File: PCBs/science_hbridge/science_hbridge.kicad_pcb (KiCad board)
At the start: 2 copper layers, 50.6 x 45 mm, 32 parts, among them J1 Conn_02x07_Odd_Even, J2 Conn_02x08_Odd_Even, J3 Conn_02x08_Odd_Even, J4 Conn_01x02_Pin, J5 Conn_01x02_Pin, J6 Conn_01x02_Pin, J7 Conn_01x04_Pin, U1 L298N, U2 MAX485E, U3 NCP718xSN500

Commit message: fixed errors, need to add quadrature
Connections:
- C1 pad 1: +5V -> +24V
- C2 pad 1: +5V -> +24V
- C6 pad 1: +24V -> +5V
- D5 pad 1: +5V -> +24V
- D6 pad 1: +5V -> +24V
- D7 pad 1: +5V -> +24V
- D8 pad 1: +5V -> +24V
- U1 pad 4: +5V -> +24V
- U1 pad 9: +24V -> +5V
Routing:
- net +5V: track 132.1 -> 128.7 mm
- net +24V: track 41.1 -> 41.8 mm
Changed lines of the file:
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@@
 			(layers "F.Cu" "F.Mask" "F.Paste")
 			(roundrect_rratio 0.25)
-			(net 47 "+5V")
+			(net 48 "+24V")
 			(pinfunction "K")
 			(pintype "passive")
@@
 			(layers "*.Cu" "*.Mask")
 			(remove_unused_layers no)
-			(net 47 "+5V")
+			(net 48 "+24V")
 			(pintype "passive")
 		)
@@
 			(layers "*.Cu" "*.Mask")
 			(remove_unused_layers no)
-			(net 47 "+5V")
+			(net 48 "+24V")
 			(pinfunction "Vs")
 			(pintype "power_in")
@@
 			(layers "*.Cu" "*.Mask")
 			(remove_unused_layers no)
-			(net 48 "+24V")
+			(net 47 "+5V")
 			(pinfunction "Vss")
 			(pintype "power_in")
@@
 			(layers "F.Cu" "F.Mask" "F.Paste")
 			(roundrect_rratio 0.25)
-			(net 47 "+5V")
+			(net 48 "+24V")
 			(pinfunction "K")
 			(pintype "passive")
@@
 			(layers "F.Cu" "F.Mask" "F.Paste")
 			(roundrect_rratio 0.25)
-			(net 47 "+5V")
+			(net 48 "+24V")
 			(pinfunction "K")
 			(pintype "passive")
@@
 			(layers "F.Cu" "F.Mask" "F.Paste")
 			(roundrect_rratio 0.25)
-			(net 47 "+5V")
+			(net 48 "+24V")
 			(pinfunction "K")
 			(pintype "passive")
@@
 			(layers "B.Cu" "B.Mask" "B.Paste")
 			(roundrect_rratio 0.212766)
-			(net 48 "+24V")
+			(net 47 "+5V")
 			(pintype "passive")
 		)
@@
 			(layers "B.Cu" "B.Mask" "B.Paste")
 			(roundrect_rratio 0.212766)
-			(net 47 "+5V")
+			(net 48 "+24V")
 			(pintype "passive")
 		)
@@
 	)
 	(segment
-		(start 161.09612 90.61388)
-		(end 163.01 88.7)
+		(start 160.72 81.14)
+		(end 160.72 83.84)
 		(width 0.75)
 		(layer "F.Cu")
@@
 	)
 	(segment
-		(start 161.984 86.374)
-		(end 156.146 86.374)
+		(start 124.01 77.4125)
+		(end 127.5 77.4125)
 		(width 0.75)
 		(layer "F.Cu")
@@
 	)
 	(segment
-		(start 124.01 77.4125)
-		(end 127.5 77.4125)
+		(start 147.974 70.5335)
+		(end 147.974 70.075124)
 		(width 0.75)
 		(layer "F.Cu")
@@
 	)
 	(segment
-		(start 147.974 70.5335)
-		(end 147.974 70.075124)
+		(start 150.43 84.88)
+		(end 148.32 82.77)
 		(width 0.75)
 		(layer "F.Cu")
@@
 	(segment
 		(start 146.22 72.2875)
-		(end 147.974 70.5335)
+		(end 148.2235 74.291)
 		(width 0.75)
 		(layer "F.Cu")
@@
 	)
 	(segment
-		(start 121.164 87.394)
-		(end 121.164 80.2585)
+		(start 146.22 72.2875)
+		(end 147.974 70.5335)
 		(width 0.75)
 		(layer "F.Cu")
@@
 	)
 	(segment
-		(start 144.91 74.21)
-		(end 133.1 74.21)
+		(start 121.164 87.394)
+		(end 121.164 80.2585)
 		(width 0.75)
 		(layer "F.Cu")
@@
 	)
 	(segment
-		(start 156.146 86.374)
-		(end 154.67 87.85)
+		(start 144.91 74.21)
+		(end 133.1 74.21)
 		(width 0.75)
 		(layer "F.Cu")
@@
 	)
 	(segment
-		(start 158.806 90.61388)
-		(end 158.81612 90.61388)
-		(width 0.75)
-		(layer "F.Cu")
-		(net 47)
-	)
-	(segment
 		(start 121.164 80.2585)
 		(end 124.01 77.4125)
@@
 	)
 	(segment
-		(start 158.49 90.94)
-		(end 158.81612 90.61388)
-		(width 0.75)
-		(layer "F.Cu")
-		(net 47)
-	)
-	(segment
 		(start 161.26 65.61)
 		(end 161.26 57.43)
@@
 	)
 	(segment
-		(start 163.01 87.4)
-		(end 161.984 86.374)
+		(start 160.72 83.84)
+		(end 159.68 84.88)
 		(width 0.75)
 		(layer "F.Cu")
@@
 	)
 	(segment
-		(start 163.01 88.7)
-		(end 163.01 87.4)
+		(start 159.68 84.88)
+		(end 150.43 84.88)
 		(width 0.75)
 		(layer "F.Cu")
@@
 	)
 	(segment
-		(start 138.09 89.59)
-		(end 139.44 90.94)
+		(start 146.22 72.9)
+		(end 144.91 74.21)
 		(width 0.75)
 		(layer "F.Cu")
@@
 	)
 	(segment
-		(start 146.22 72.9)
-		(end 144.91 74.21)
+		(start 153.871 74.291)
+		(end 160.72 81.14)
 		(width 0.75)
 		(layer "F.Cu")
@@
 	)
 	(segment
-		(start 139.44 90.94)
-		(end 158.49 90.94)
-		(width 0.75)
-		(layer "F.Cu")
-		(net 47)
-	)
-	(segment
 		(start 133.1 74.21)
 		(end 130.38 76.93)
@@
 	)
 	(segment
-		(start 127.63 77.5425)
-		(end 130.15 77.5425)
+		(start 148.2235 74.291)
+		(end 153.871 74.291)
 		(width 0.75)
 		(layer "F.Cu")
@@
 	)
 	(segment
-		(start 158.81612 90.61388)
-		(end 161.09612 90.61388)
+		(start 127.63 77.5425)
+		(end 130.15 77.5425)
 		(width 0.75)
 		(layer "F.Cu")
@@
 	)
 	(segment
-		(start 155.1025 87.479)
-		(end 154.47 88.1115)
-		(width 0.75)
+		(start 148.1 84.6075)
+		(end 148.1 82.99)
+		(width 1)
 		(layer "B.Cu")
 		(net 47)
 	)
 	(segment
-		(start 154.7025 85.315)
-		(end 154.7025 87.8175)
+		(start 148.5525 85.06)
+		(end 148.1 84.6075)
 		(width 1)
 		(layer "B.Cu")
@@
 	)
 	(segment
-		(start 154.7025 87.8175)
-		(end 154.67 87.85)
+		(start 148.1 82.99)
+		(end 148.32 82.77)
 		(width 1)
 		(layer "B.Cu")
@@
 	)
 	(segment
-		(start 159.85 85.11)
-		(end 150.66 85.11)
+		(start 163.01 86.63)
+		(end 163.01 87.4)
 		(width 1)
 		(layer "F.Cu")
@@
 	)
 	(segment
-		(start 160.67 83.51)
-		(end 160.67 84.29)
+		(start 161.859 86.249)
+		(end 156.271 86.249)
 		(width 1)
 		(layer "F.Cu")
@@
 	)
 	(segment
-		(start 160.67 84.29)
-		(end 159.85 85.11)
+		(start 162.97 86.59)
+		(end 163.01 86.63)
 		(width 1)
 		(layer "F.Cu")
@@
 	)
 	(segment
-		(start 151.4875 72.43)
-		(end 152.7925 72.43)
-		(width 0.75)
-		(layer "F.Cu")
-		(net 48)
-	)
-	(segment
-		(start 150.66 85.11)
-		(end 148.32 82.77)
+		(start 159.02 71.98)
+		(end 162.97 75.93)
 		(width 1)
 		(layer "F.Cu")
@@
 	)
 	(segment
-		(start 160.7 83.48)
-		(end 160.67 83.51)
-		(width 1)
+		(start 151.4875 72.43)
+		(end 152.7925 72.43)
+		(width 0.75)
 		(layer "F.Cu")
 		(net 48)
@@
 	)
 	(segment
-		(start 153.49 73.1275)
-		(end 157.8725 73.1275)
-		(width 0.75)
+		(start 156.271 86.249)
+		(end 154.67 87.85)
+		(width 1)
 		(layer "F.Cu")
 		(net 48)
 	)
 	(segment
-		(start 160.7 73.66)
-		(end 160.7 83.48)
-		(width 1)
+		(start 153.49 73.1275)
+		(end 157.8725 73.1275)
+		(width 0.75)
 		(layer "F.Cu")
 		(net 48)
 	)
 	(segment
-		(start 159.02 71.98)
-		(end 160.7 73.66)
+		(start 162.97 75.93)
+		(end 162.97 86.59)
 		(width 1)
 		(layer "F.Cu")
@@
 	)
 	(segment
-		(start 148.1 84.6075)
-		(end 148.1 82.99)
+		(start 163.01 87.4)
+		(end 161.859 86.249)
 		(width 1)
-		(layer "B.Cu")
+		(layer "F.Cu")
 		(net 48)
 	)
@@
 	)
 	(segment
-		(start 148.5525 85.06)
-		(end 148.1 84.6075)
+		(start 155.1025 87.479)
+		(end 154.47 88.1115)
+		(width 0.75)
+		(layer "B.Cu")
+		(net 48)
+	)
+	(segment
+		(start 154.7025 85.315)
+		(end 154.7025 87.8175)
 		(width 1)
 		(layer "B.Cu")
@@
 	)
 	(segment
-		(start 148.1 82.99)
-		(end 148.32 82.77)
+		(start 154.7025 87.8175)
+		(end 154.67 87.85)
 		(width 1)
 		(layer "B.Cu")

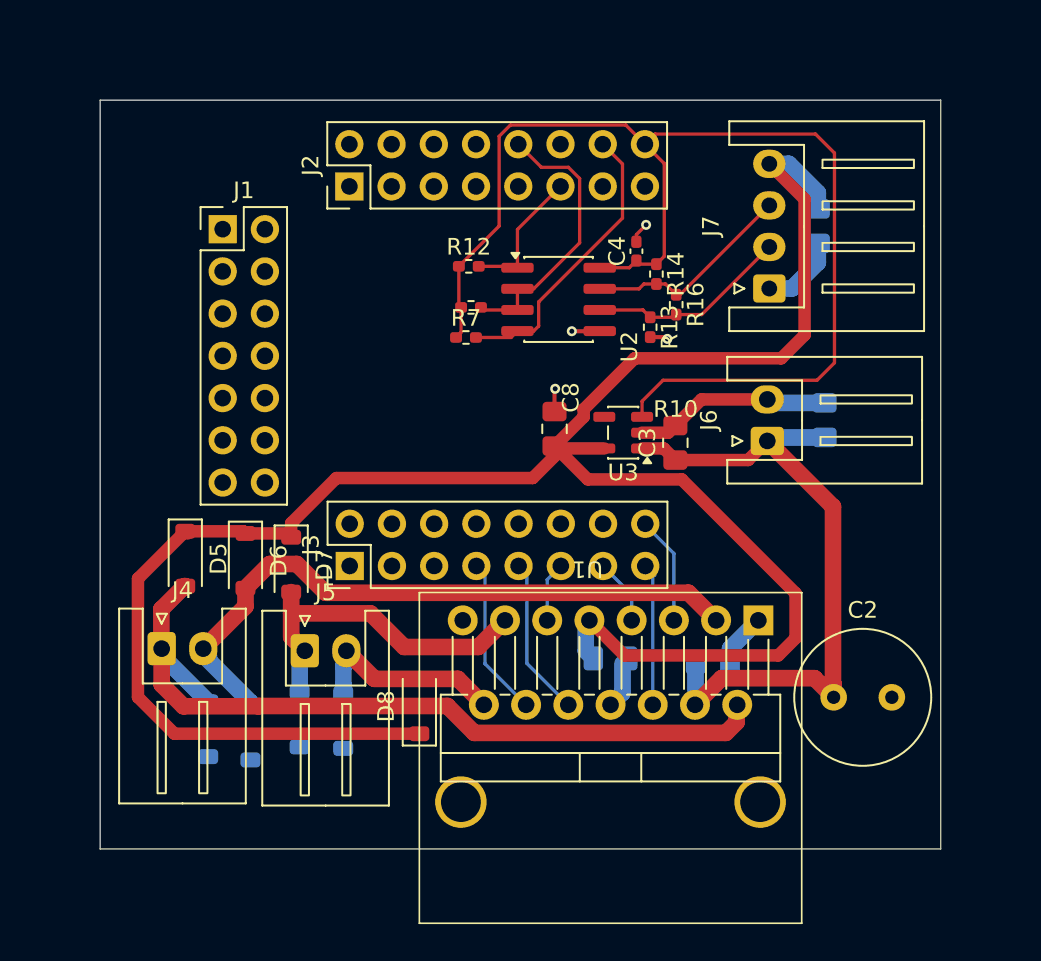
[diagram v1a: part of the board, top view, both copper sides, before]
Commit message: fixed both boards, just needs mounting + silkscreen, ready to review
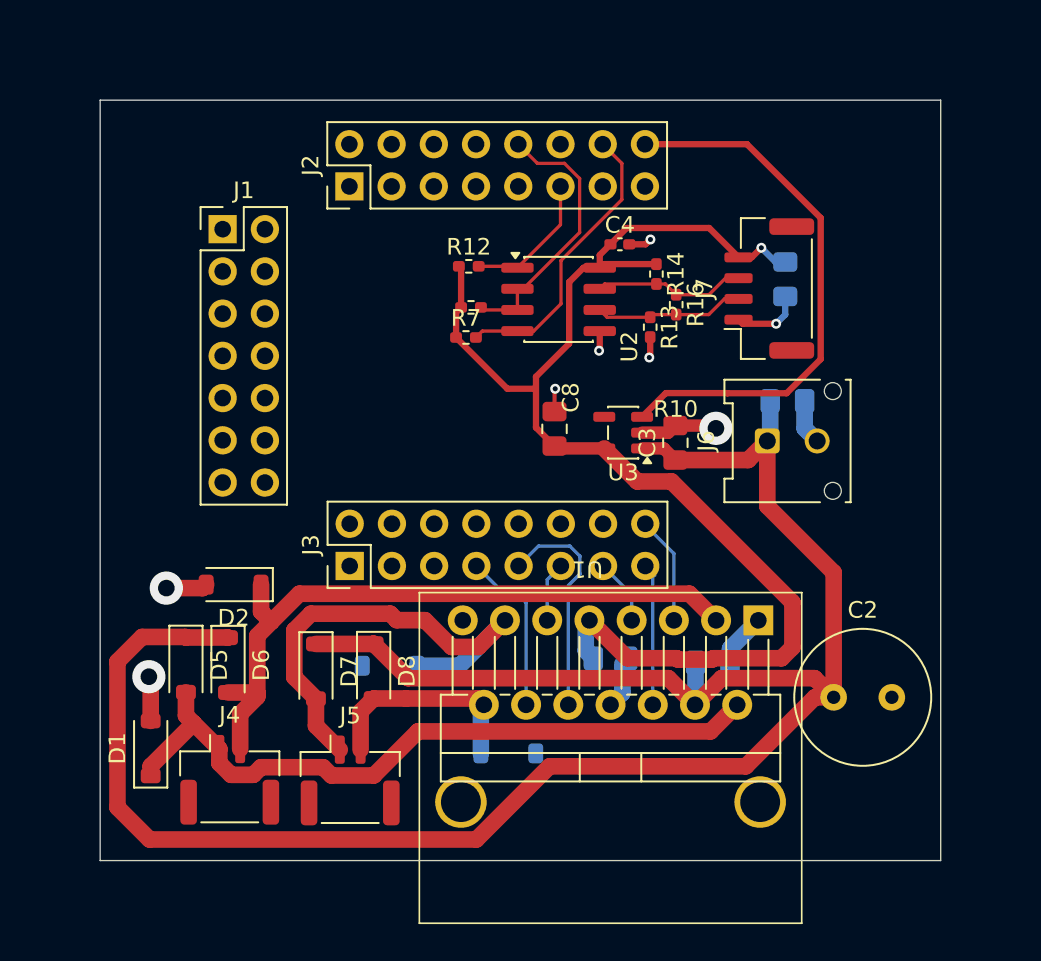
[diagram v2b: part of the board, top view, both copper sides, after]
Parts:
- D1, D2: moved to F.Cu
- J4, J5: footprint Connector_JST:JST_XH_S2B-XH-A_1x02_P2.50mm_Horizontal -> Connector_JST:JST_GH_SM02B-GHS-TB_1x02-1MP_P1.25mm_Horizontal
- J6: footprint Connector_JST:JST_XH_S2B-XH-A_1x02_P2.50mm_Horizontal -> Connector_Molex:Molex_Micro-Fit_3.0_43045-0212_2x01_P3.00mm_Vertical
- J7: footprint Connector_JST:JST_XH_S4B-XH-A_1x04_P2.50mm_Horizontal -> Connector_JST:JST_GH_SM04B-GHS-TB_1x04-1MP_P1.25mm_Horizontal
- moved D4 10.1 mm to (143.4, 90.8), turned to 0 degrees
- moved D2 8.95 mm to (126.9, 80.6), turned to 180 degrees
- moved J4 8.89 mm to (126.7, 92.4)
- moved J5 8.26 mm to (133.9, 92.4)
- moved D7 6.59 mm to (131.9, 85.8)
- moved D5 6.39 mm to (124.0, 85.5)
- moved D6 6.35 mm to (126.6, 85.5)
- moved D3 6.31 mm to (136.3, 85.5), turned to 180 degrees
- moved C7 3.74 mm to (160.1, 62.2)
- moved D1 3.65 mm to (121.9, 90.5), turned to 90 degrees
- moved D8 3.47 mm to (135.3, 85.8), turned to -90 degrees
- moved C9 2.51 mm to (160.2, 69.6), turned to 0 degrees
- moved C4 1.08 mm to (150.2, 60.1), turned to 0 degrees
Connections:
- C4 pad 1: +3.3V -> +5V
- R10 pad 1: +3.3V -> +5V
- R12 pad 1: +3.3V -> +5V
- R14 pad 1: +3.3V -> +5V
- R7 pad 1: +3.3V -> +5V
- U2 pad 8: +3.3V -> +5V
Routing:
- net +24V: track 41.8 -> 128.6 mm
- net +5V: track 128.7 -> 78.3 mm, vias 0 -> 1
- net +3.3V: track 72.6 -> 33.1 mm
- net Net-(D3-K): track 21.3 -> 29.3 mm
- net Net-(D1-K): track 48.1 -> 42.5 mm
- net /28: track 9.59 -> 14.4 mm
- net signal_2 +: track 12.8 -> 9.15 mm
- net signal_2 -: track 12.2 -> 8.99 mm
- net Net-(D2-K): track 39.6 -> 40.8 mm
- net Net-(D4-K): track 12.3 -> 13.2 mm
- net GND: track 28.0 -> 28.1 mm, vias 4 -> 8
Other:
- board size 50.6 x 45 mm -> 50.6 x 45.7 mm

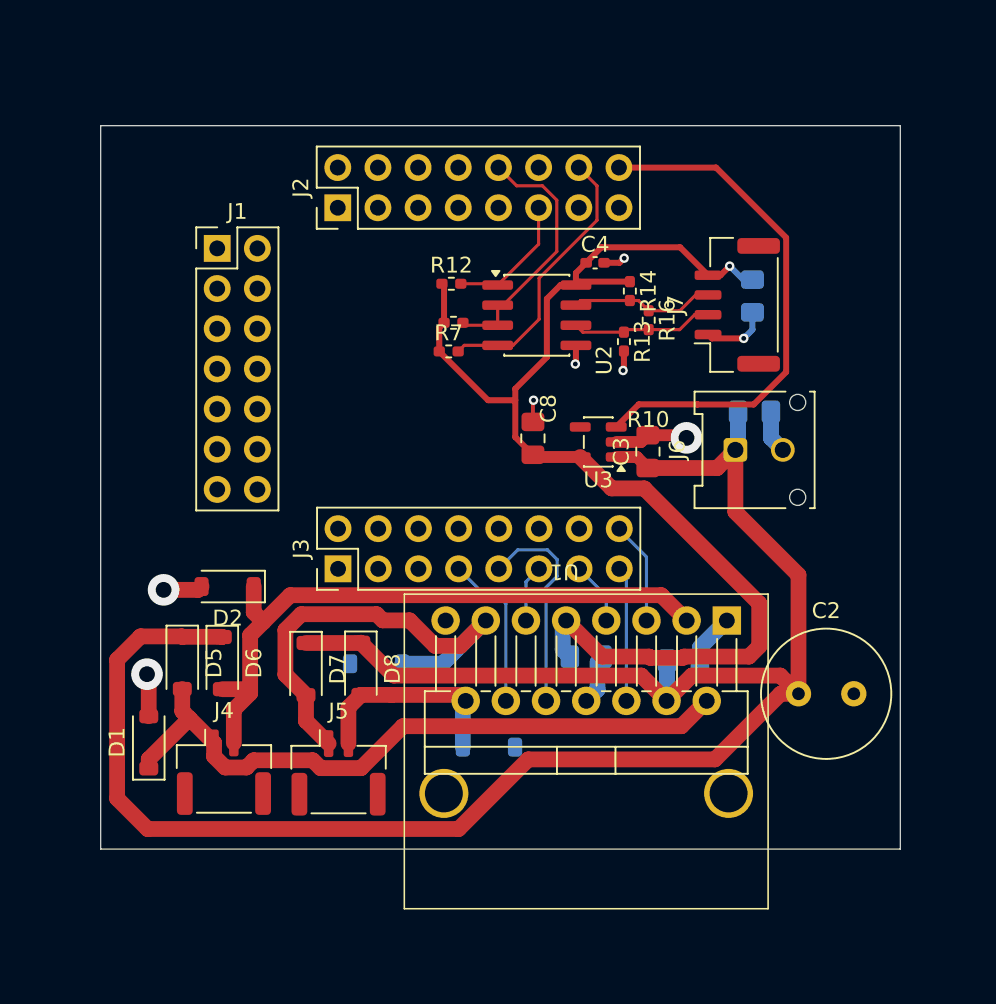
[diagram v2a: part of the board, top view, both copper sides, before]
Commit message: added quadrature and mounting holes
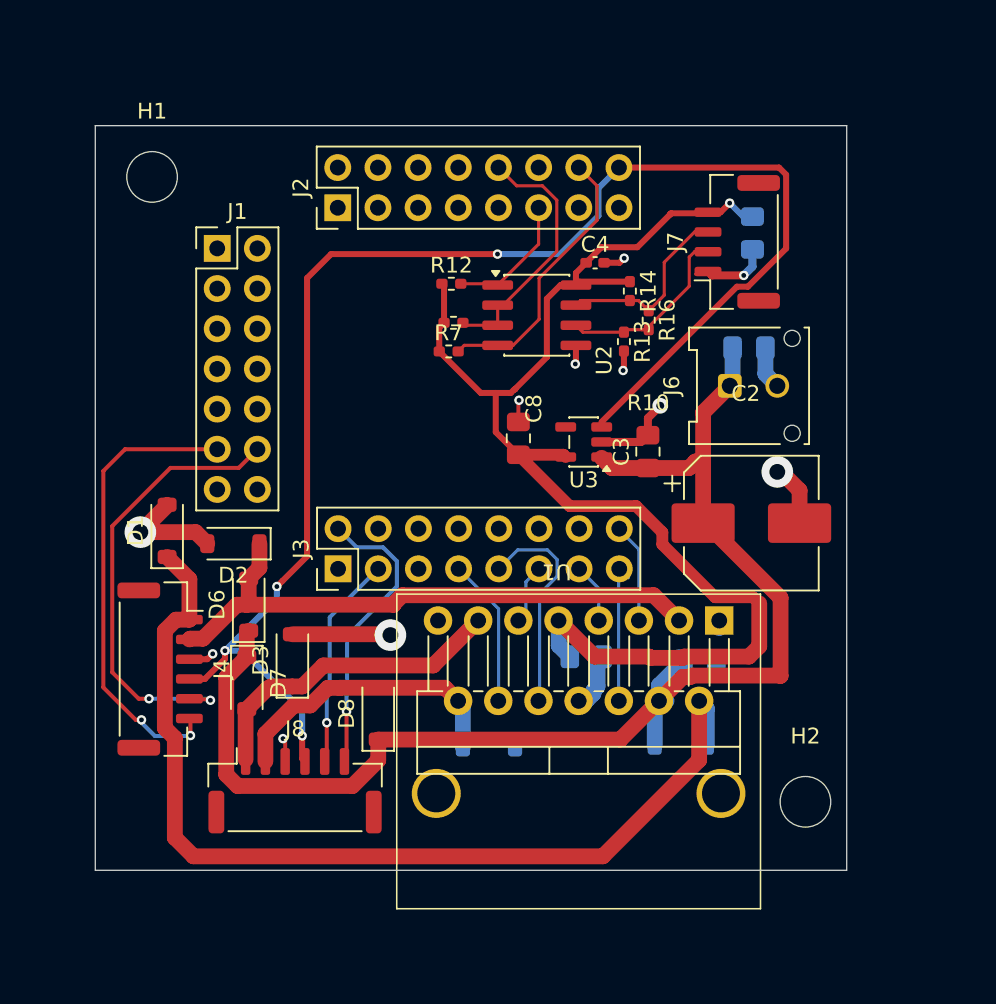
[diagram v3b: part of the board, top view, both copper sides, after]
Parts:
- removed J5: Conn_01x02_Pin, Connector_JST:JST_GH_SM02B-GHS-TB_1x02-1MP_P1.25mm_Horizontal
- added H1: MountingHole, MountingHole:MountingHole_3.2mm_M3, F.Cu at (122.1, 54.7)
- added H2: MountingHole, MountingHole:MountingHole_3.2mm_M3, F.Cu at (163.4, 94.2)
- added J8: Conn_01x06, Connector_JST:JST_GH_SM06B-GHS-TB_1x06-1MP_P1.25mm_Horizontal, F.Cu at (131.2, 93.5)
- C2: footprint Capacitor_THT:C_Radial_D8.0mm_H7.0mm_P3.50mm -> Capacitor_SMD:CP_Elec_8x6.2
- D3: moved to F.Cu
- D5: moved to B.Cu
- J4: value Conn_01x02_Pin -> Conn_01x06; footprint Connector_JST:JST_GH_SM02B-GHS-TB_1x02-1MP_P1.25mm_Horizontal -> Connector_JST:JST_GH_SM06B-GHS-TB_1x06-1MP_P1.25mm_Horizontal
- moved D5 31.9 mm to (155.6, 90.7), turned to 0 degrees
- moved D1 13.4 mm to (123.1, 77.1)
- moved C2 11.2 mm to (160.0, 76.6)
- moved J4 7.67 mm to (122.7, 85.8), turned to -90 degrees
- moved D3 5.30 mm to (131.0, 85.3), turned to 90 degrees
- moved J6 4.07 mm to (158.7, 67.9)
- moved C9 4.07 mm to (159.9, 65.5)
- moved D6 4.05 mm to (128.2, 81.8), turned to 90 degrees
- moved C7 3.98 mm to (160.1, 58.3)
- moved J7 3.98 mm to (159.1, 58.8)
- moved D7 3.84 mm to (128.1, 86.7)
- moved D8 3.03 mm to (136.4, 88.6), turned to 90 degrees
- moved D2 2.73 mm to (127.3, 77.9)
- moved C1 1.04 mm to (156.8, 85.3)
- moved C8 0.92 mm to (145.3, 71.2)
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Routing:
- net +3.3V: track 33.1 -> 94.3 mm, vias 0 -> 4
- net +24V: track 128.6 -> 85.8 mm
- net /23: track 0.00 -> 29.5 mm, vias 0 -> 2
- net /22: track 0.00 -> 28.8 mm, vias 0 -> 2
- net Net-(D1-K): track 42.5 -> 62.6 mm
- net /42: track 0.00 -> 18.6 mm, vias 0 -> 1
- net GND: track 28.1 -> 42.2 mm, vias 8 -> 11
- net /41: track 0.00 -> 13.5 mm, vias 0 -> 1
- net Net-(D3-K): track 29.3 -> 20.2 mm
- net Net-(D4-K): track 13.2 -> 18.5 mm
- net +5V: track 78.3 -> 83.2 mm
- net Net-(D2-K): track 40.8 -> 37.0 mm
- net signal_2 -: track 8.99 -> 12.2 mm
- net signal_2 +: track 9.15 -> 12.0 mm
- net /33: track 3.98 -> 3.30 mm
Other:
- board size 50.6 x 45.7 mm -> 47.5 x 47.1 mm

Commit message: silkscreen
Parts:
- moved D7 3.87 mm to (131.3, 84.5)
- moved D3 3.04 mm to (134.0, 84.6)
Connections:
- R12 pad 2: /52 -> /54
- R7 pad 2: /51 -> /53
- U2 pad 1: /52 -> /54
- U2 pad 4: /51 -> /53
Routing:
- net /51: track 17.5 -> 0.00 mm
- net /53: track 0.00 -> 16.5 mm
- net /52: track 8.33 -> 0.00 mm
- net /54: track 0.00 -> 7.98 mm
- net +24V: track 85.8 -> 89.1 mm
- net GND: track 42.2 -> 39.6 mm
- net /55: track 16.5 -> 13.9 mm
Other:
- board text added: "+24V GND"
- board text added: "100n"
- board text added: "10k"
- board text added: "10u"
- board text added: "120"
- board text added: "1uf"
- board text added: "20k"
- board text added: "A B VCC GND M+ M-"
